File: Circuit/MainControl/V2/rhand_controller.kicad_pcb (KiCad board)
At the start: 2 copper layers, 100 x 100 mm, 37 parts, among them J1 R_Hand, J2 L_Hand, P1 BLUETOOTH, P10 LV_ADC, P11 LW_ADC, P12 RU_ADC, P13 RV_ADC, P14 RW_ADC, P2 CONN_01X06, P9 LU_ADC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

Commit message: 配置をちょっとした
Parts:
- moved R3 166.8 mm to (38.0, 77.5), turned to 180 degrees
- moved R1 166.3 mm to (38.0, 72.4), turned to 180 degrees
- moved R2 163.0 mm to (38.0, 75.0), turned to 180 degrees
- moved R7 148.1 mm to (76.0, 79.0)
- moved S1 138.9 mm to (41.0, 80.0), turned to 180 degrees
- moved R6 115.8 mm to (72.0, 69.5), turned to 180 degrees
- moved R10 113.1 mm to (95.0, 81.5)
- moved R8 109.5 mm to (95.0, 61.0)
- moved P1 85.8 mm to (70.0, 56.0)
- moved P2 80.4 mm to (146.2, 95.0)
- moved SW1 57.5 mm to (138.0, 47.0), turned to 180 degrees
- moved C2 56.8 mm to (143.0, 66.0)
- moved R4 51.7 mm to (136.5, 39.5)
- moved R12 23.5 mm to (153.0, 73.0), turned to 180 degrees
- moved P9 18.6 mm to (113.0, 112.0)
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
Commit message: ラベル名のつけ方変更
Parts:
- SW1: footprint YASU:XA_2Pin -> YASU:XA_2Pin_LP
- moved D1 135.3 mm to (58.2, 38.7)
- moved R5 124.3 mm to (65.6, 46.3), turned to 90 degrees
- moved U1 112.3 mm to (59.7, 51.4)
- moved C1 88.2 mm to (83.7, 37.5), turned to 180 degrees
- moved C2 70.8 mm to (80.6, 99.4), turned to 135 degrees
- moved U2 28.6 mm to (75.5, 104.5)
- moved R6 27.5 mm to (78.9, 96.1)
- moved J1 25.6 mm to (110.5, 88.4), turned to 0 degrees
- moved R1 25.3 mm to (54.0, 92.0)
- moved R3 25.3 mm to (54.0, 97.1)
- moved R8 25.2 mm to (110.5, 80.9), turned to 180 degrees
- moved R2 25.2 mm to (54.0, 94.5)
- moved S1 23.3 mm to (57.0, 97.0)
- moved J2 21.8 mm to (110.5, 103.4), turned to 0 degrees
- moved R10 21.2 mm to (110.5, 95.9), turned to 180 degrees
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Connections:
- S1 pad 1: Net-(S1-Pad1) -> /DSW_B0
- S1 pad 2: /DSW_B0 -> /DSW_B1
- S1 pad 3: /DSW_B1 -> /DSW_B2
- S1 pad 4: /DSW_B2 -> Net-(S1-Pad4)
- S1 pad 5: +3V3 -> Net-(S1-Pad5)
- S1 pad 8: Net-(S1-Pad8) -> +3V3
- U2 pad 6: /Move_X -> /Move_Y
- U2 pad 7: /Move_Y -> /Move_X
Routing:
- net GND: track 0.00 -> 79.8 mm
- net +3V3: track 0.00 -> 75.0 mm
- net /RightW: track 0.00 -> 42.8 mm
- net /LeftU: track 0.00 -> 41.6 mm
- net /RightV: track 0.00 -> 28.6 mm
- net /LeftV: track 0.00 -> 28.4 mm
- net /RightU: track 0.00 -> 14.5 mm
- net /LeftW: track 0.00 -> 14.2 mm
- net Net-(R6-Pad2): track 0.00 -> 4.34 mm
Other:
- net class Default: clearance 0.2 -> 0.1; trace_width 0.25 -> 0.5; via_dia 0.6 -> 1.6; via_drill 0.4 -> 0.8
- rule trace_clearance: 0.2 -> 0.1
- rule trace_min: 0.2 -> 0.5
- rule via_min_drill: 0.3 -> 0.8
- rule via_min_size: 0.4 -> 1.6

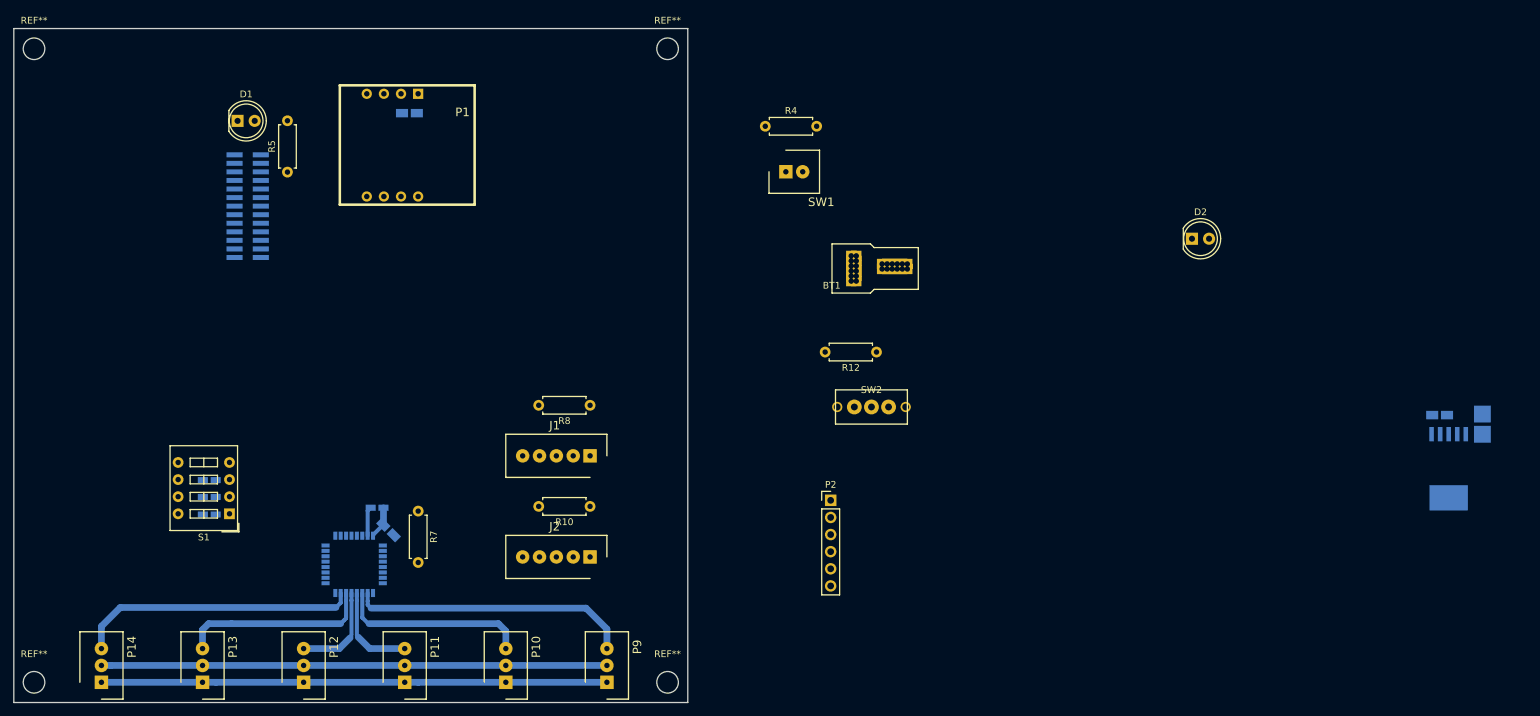
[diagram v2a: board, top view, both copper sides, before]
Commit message: 配線が半分完了,電源と無線モジュールが未配線
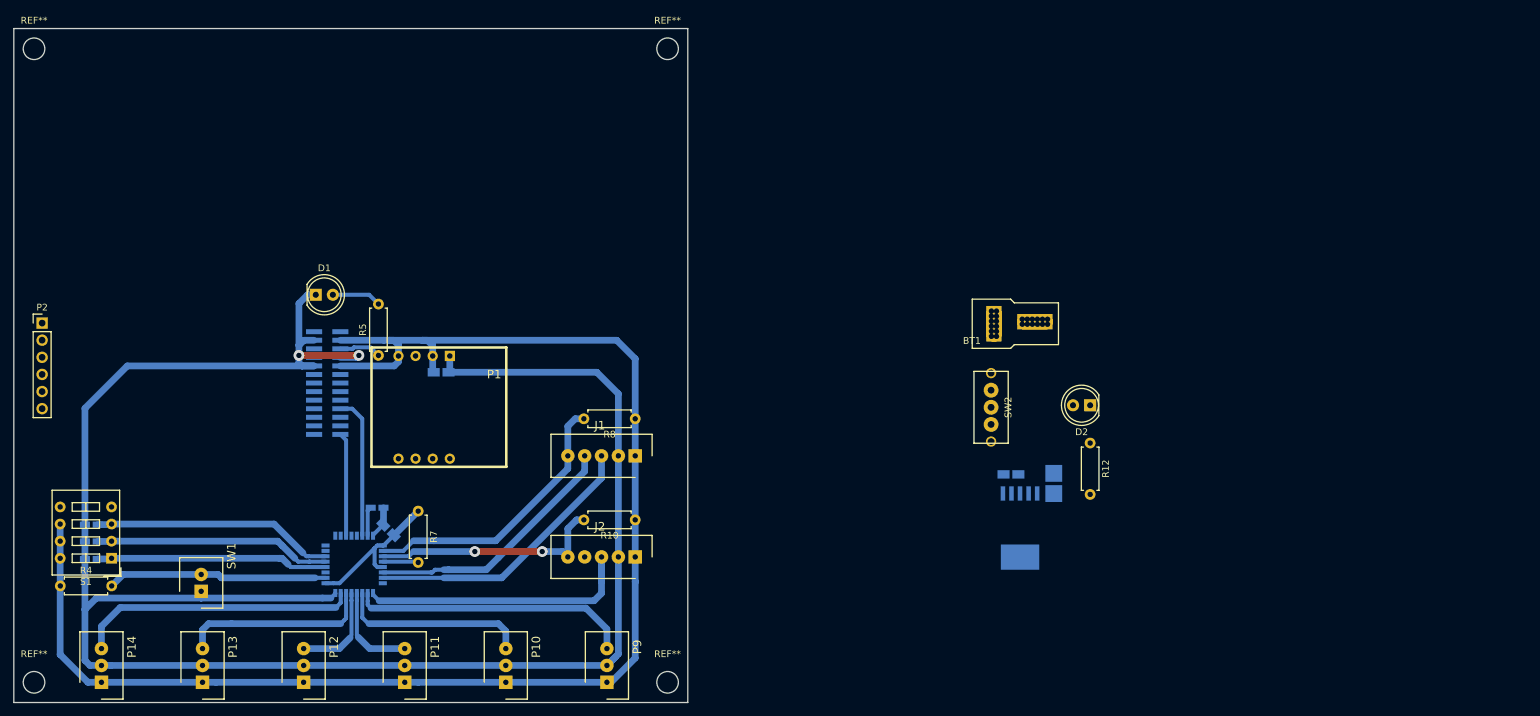
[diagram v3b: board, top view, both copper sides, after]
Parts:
- U1: footprint YASU:Pin_Header_Straight_2x13_Pitch1.27mm_SMD_foIM315 -> YASU:IM315
- moved R4 124.9 mm to (31.9, 107.7)
- moved P2 119.9 mm to (29.2, 68.7)
- moved SW1 106.8 mm to (52.8, 108.5), turned to 270 degrees
- moved C3 64.2 mm to (172.9, 91.2)
- moved C4 64.2 mm to (179.3, 92.5)
- moved U3 64.2 mm to (174.3, 94.5)
- moved P1 39.2 mm to (87.2, 81.2)
- moved C1 38.7 mm to (88.4, 76.0)
- moved R12 34.5 mm to (184.7, 86.5), turned to 270 degrees
- moved R5 30.4 mm to (79.1, 73.5)
- moved D2 29.0 mm to (184.7, 80.9), turned to 180 degrees
- moved U1 28.8 mm to (71.5, 77.6)
- moved D1 28.3 mm to (69.8, 64.5)
- moved BT1 22.4 mm to (170.4, 68.8)
- moved R3 18.7 mm to (36.5, 103.7)
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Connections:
- net Net-(R6-Pad2) renamed /BOOT
- U2 pad 2: /Enable_L -> /Enable_R
- U2 pad 3: /Enable_R -> /Enable_L
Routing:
- net GND: track 79.8 -> 298.4 mm, vias 0 -> 2
- net +3V3: track 75.0 -> 238.3 mm
- net /Rotation: track 0.00 -> 44.1 mm
- net /Move_X: track 0.00 -> 41.9 mm
- net /Enable_R: track 0.00 -> 41.6 mm
- net /Move_Y: track 0.00 -> 38.5 mm
- net /DSW_B2: track 0.00 -> 35.8 mm
- net /Enable_L: track 0.00 -> 35.2 mm, vias 0 -> 2
- net /DSW_B1: track 0.00 -> 35.2 mm
- net /DSW_B0: track 0.00 -> 34.4 mm
- net /Em_SW: track 0.00 -> 32.6 mm
- net /315MHz_TXD: track 0.00 -> 21.2 mm
- net /busy: track 0.00 -> 15.4 mm
- net Net-(D1-Pad2): track 0.00 -> 7.33 mm
- net Net-(R5-Pad1): track 0.00 -> 6.27 mm
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
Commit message: コミット編集しようとしたら全部破棄されたからやる気失った
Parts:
- moved BT1 141.0 mm to (29.8, 79.7), turned to 270 degrees
- moved SW2 139.3 mm to (31.4, 67.5), turned to 90 degrees
- moved P2 93.2 mm to (121.7, 57.2)
- moved U3 84.5 mm to (96.2, 62.3), turned to 270 degrees
- moved C4 82.5 mm to (101.7, 64.4), turned to 0 degrees
- moved C3 79.6 mm to (99.5, 60.4), turned to 270 degrees
- moved R12 79.2 mm to (107.6, 68.6), turned to 180 degrees
- moved D2 77.6 mm to (108.7, 65.0), turned to 90 degrees

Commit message: 回路設計完了
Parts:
- moved REF** 29.0 mm to (122.0, 57.0)
- moved REF** 29.0 mm to (28.0, 57.0)
- moved P2 18.8 mm to (123.4, 75.9), turned to 180 degrees
- moved R12 0.20 mm to (107.8, 68.6)
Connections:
- J2 pad 3: /Rotation -> /LHand/Joy_Y
- J2 pad 4: /LHand/Joy_Y -> /Rotation
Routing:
- net GND: track 298.4 -> 391.8 mm
- net +7.4V: track 0.00 -> 76.6 mm
- net +3V3: track 238.3 -> 311.0 mm, vias 0 -> 2
- net /reset315: track 0.00 -> 36.4 mm, vias 0 -> 2
- net /315MHz_RXD: track 0.00 -> 29.7 mm, vias 0 -> 2
- net /Blutooth_RXD: track 0.00 -> 29.4 mm, vias 0 -> 2
- net /Blutooth_TXD: track 0.00 -> 25.6 mm, vias 0 -> 2
- net Net-(BT1-Pad1): track 0.00 -> 12.3 mm
- net /SWDIO: track 0.00 -> 9.06 mm
- net /NRST: track 5.30 -> 13.2 mm
- net /SWO: track 0.00 -> 7.50 mm
- net /SWCLK: track 0.00 -> 7.43 mm
- net /Rotation: track 44.1 -> 37.3 mm
- net Net-(D2-Pad1): track 0.00 -> 3.97 mm
- net /busy: track 15.4 -> 15.9 mm
- added copper zone on B.Cu, net +3V3
- added copper zone on B.Cu, net GND
- added copper zone on B.Cu, net Net-(BT1-Pad1)
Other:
- board size 100 x 100 mm -> 100 x 71 mm
